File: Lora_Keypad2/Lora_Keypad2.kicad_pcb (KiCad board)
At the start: 2 copper layers, 53.3 x 76.2 mm, 7 parts, among them J1 OLED Conn

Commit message: update
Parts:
- added R3: 4.7K, Resistor_THT:R_Axial_DIN0207_L6.3mm_D2.5mm_P7.62mm_Horizontal, F.Cu at (203.5, 60.5)
- added R4: 4.7K, Resistor_THT:R_Axial_DIN0207_L6.3mm_D2.5mm_P7.62mm_Horizontal, F.Cu at (203.5, 57.4)
- moved R2 1.80 mm to (199.9, 57.4)
- moved J1 0.94 mm to (199.8, 63.5)
- moved R1 0.32 mm to (199.9, 60.5)
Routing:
- net +3.3V: track 77.7 -> 83.3 mm
- net I2C_SDA: track 26.3 -> 31.4 mm
- net I2C_SCL: track 24.1 -> 27.4 mm
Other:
- board size 53.3 x 76.2 mm -> 54 x 76.2 mm

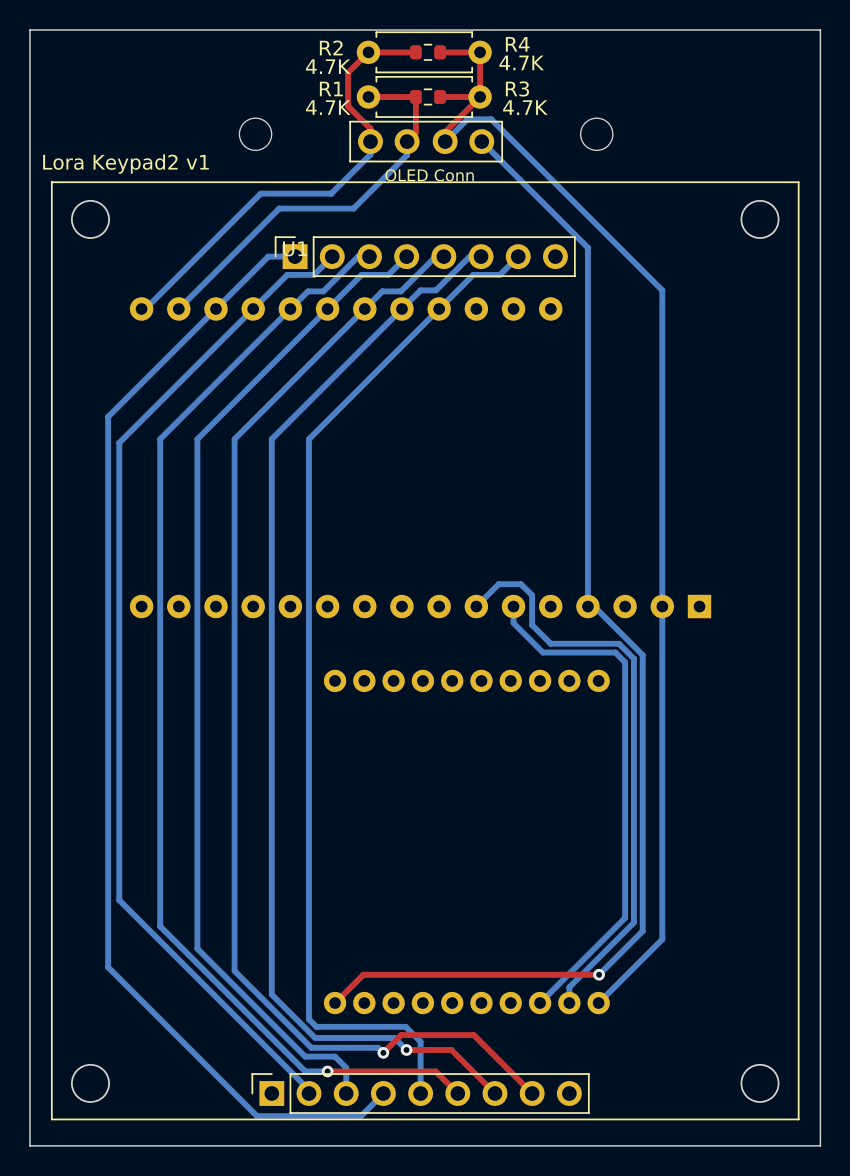
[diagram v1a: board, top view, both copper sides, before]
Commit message: add plug in 3 to 4 adapter
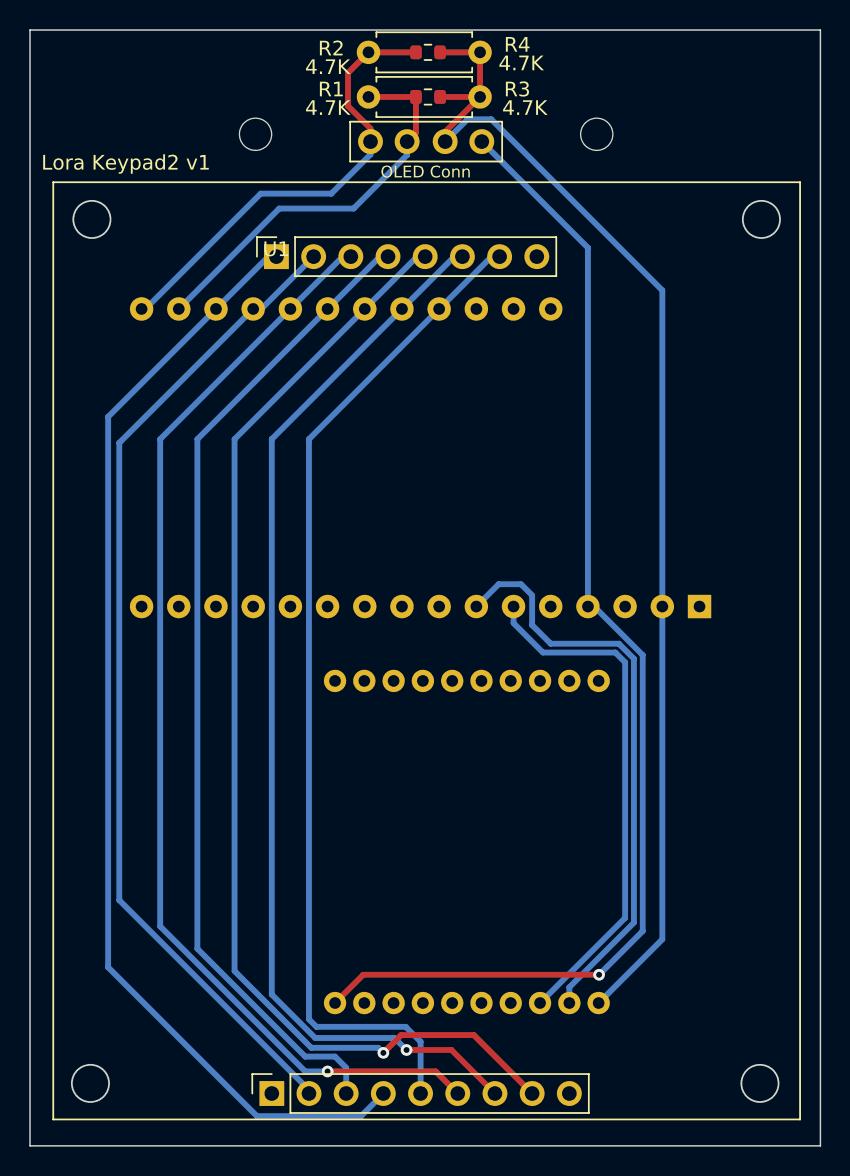
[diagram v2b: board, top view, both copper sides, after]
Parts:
- moved U1 1.27 mm to (189.5, 71.4)
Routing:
- net C2: track 69.6 -> 68.3 mm
- net R4: track 70.9 -> 69.6 mm
- net R3: track 75.4 -> 74.1 mm
- net R1: track 69.5 -> 68.3 mm
- net C3: track 77.8 -> 76.5 mm
- net R2: track 80.6 -> 79.3 mm
- net C1: track 78.5 -> 77.3 mm
